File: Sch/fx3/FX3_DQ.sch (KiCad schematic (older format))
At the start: 22 parts, among them IC1 CYUSB3014, J1 JP4, J2 Header5, P1 CONN_02X40, P2 CONN_02X40, U1 LTC2292

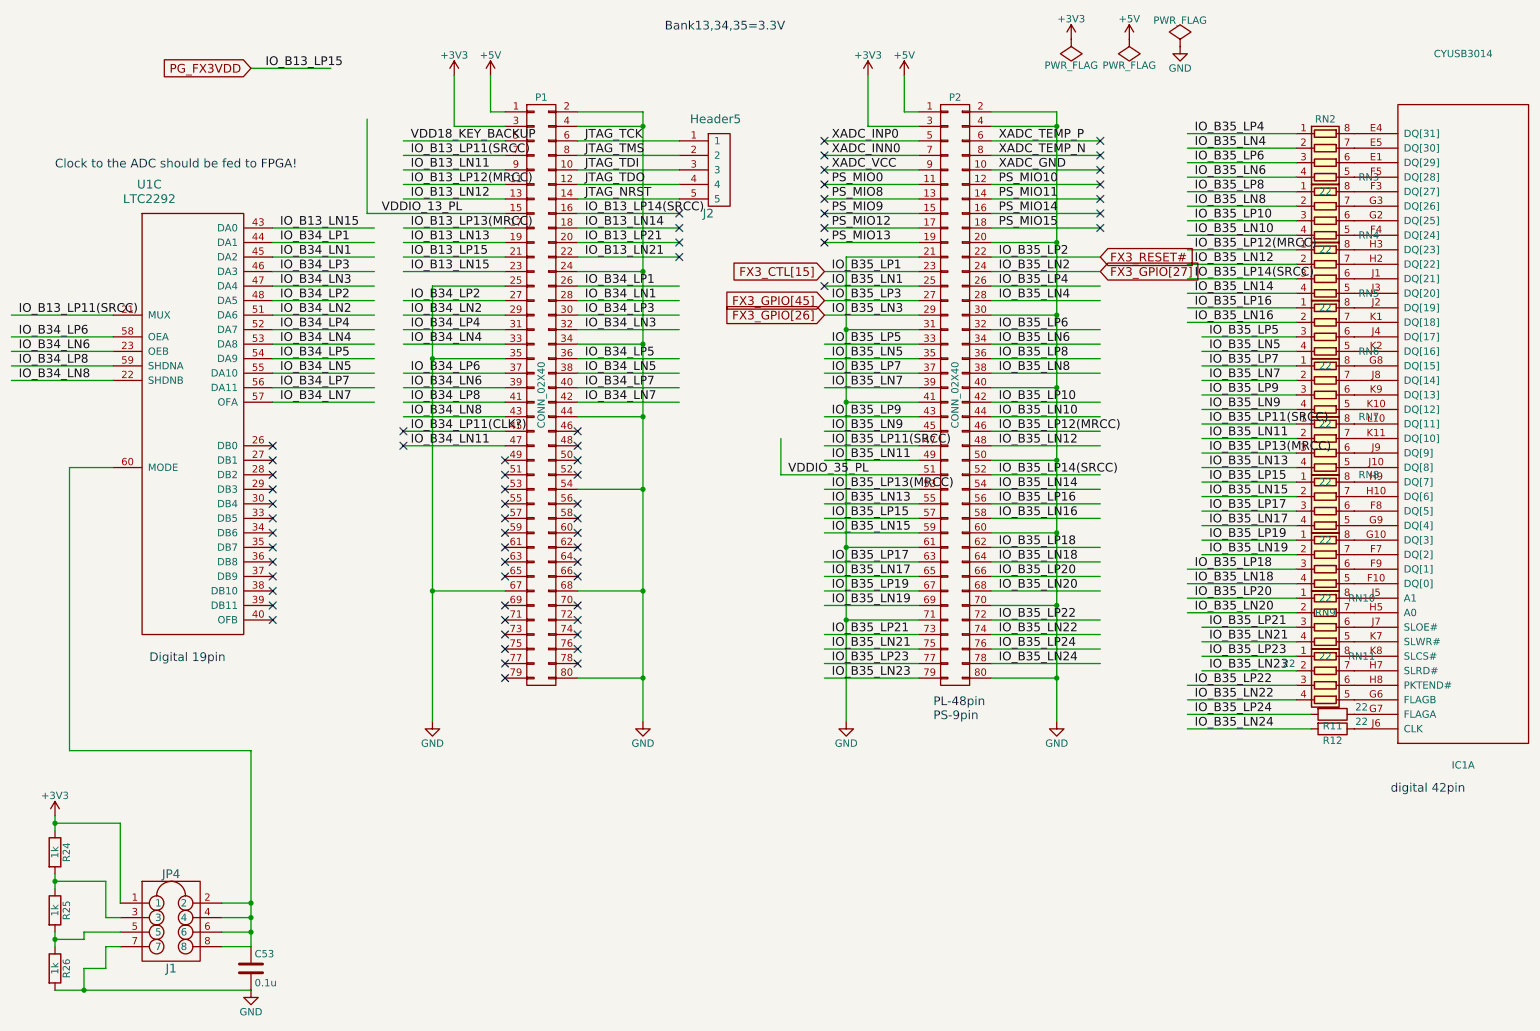
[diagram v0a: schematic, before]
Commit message: separate FX3 and ADC
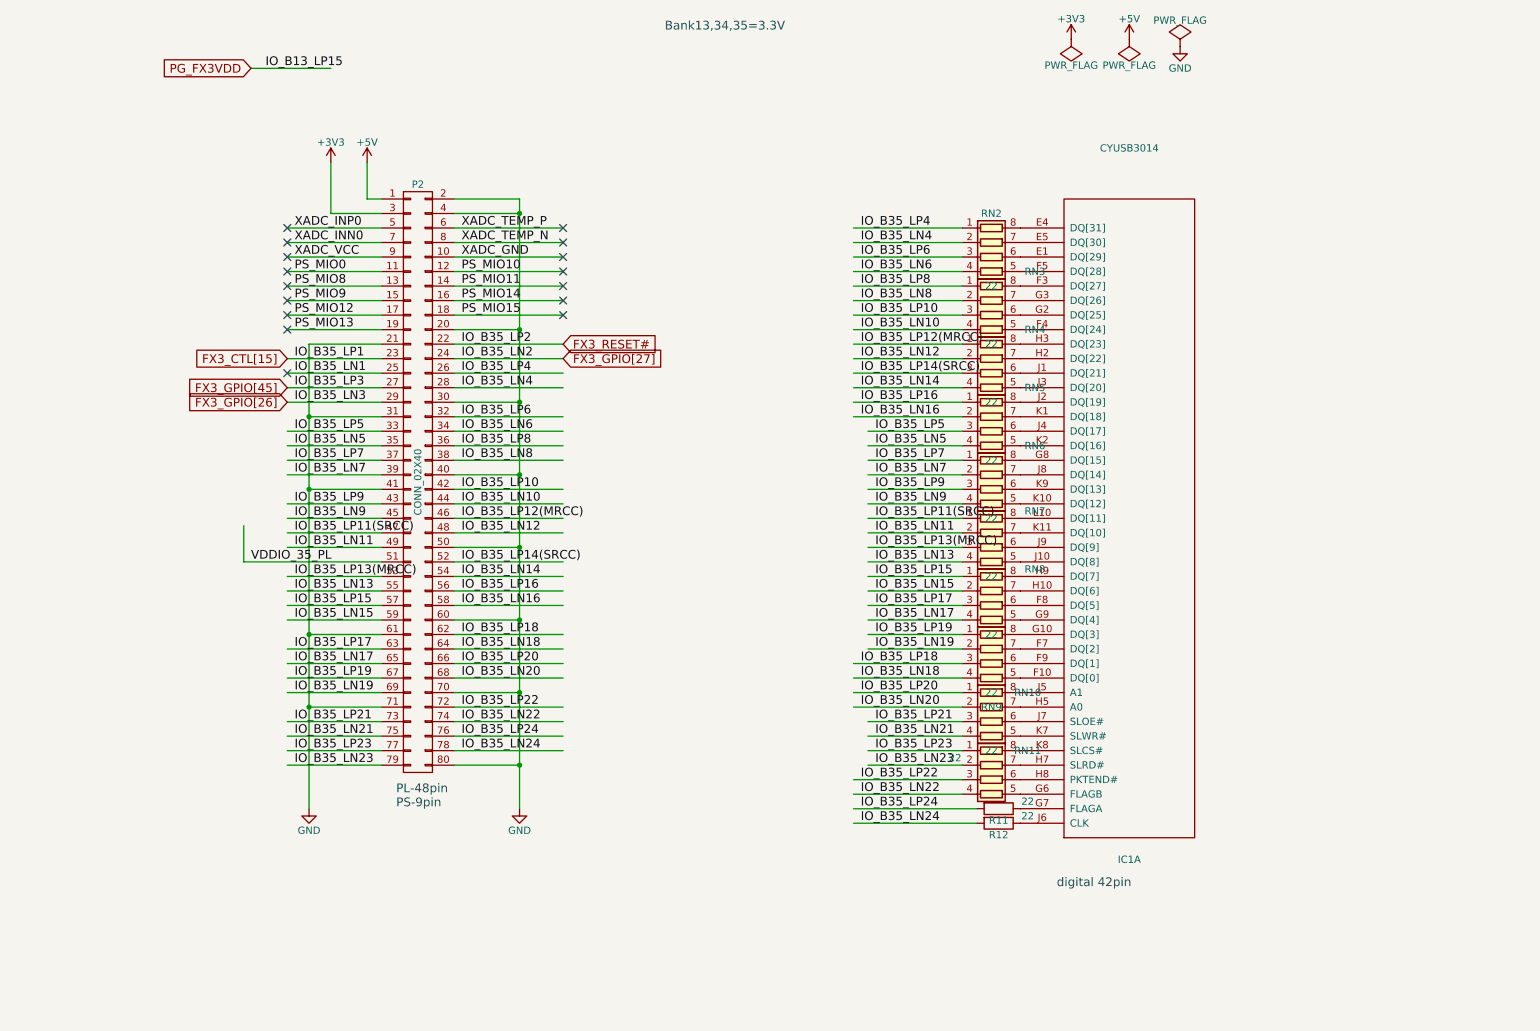
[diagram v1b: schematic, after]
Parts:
- removed C53: 0.1u, symbol C
- removed J1: JP4, symbol JP4
- removed J2: Header5, symbol Header5
- removed P1: CONN_02X40, symbol CONN_02X40
- removed R24, R25, R26: 1k, symbol R
- removed U1: LTC2292, symbol LTC2292
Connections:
- net labels removed: IO_B13_LN11, IO_B13_LN12, IO_B13_LN13, IO_B13_LN14, IO_B13_LN15, IO_B13_LN21, IO_B13_LP11(SRCC), IO_B13_LP12(MRCC), IO_B13_LP13(MRCC), IO_B13_LP14(SRCC), IO_B13_LP21, IO_B34_LN1, IO_B34_LN11, IO_B34_LN2, IO_B34_LN3, IO_B34_LN4, IO_B34_LN5, IO_B34_LN6, IO_B34_LN7, IO_B34_LN8, IO_B34_LP1, IO_B34_LP11(CLK?), IO_B34_LP2, IO_B34_LP3, IO_B34_LP4, IO_B34_LP5, IO_B34_LP6, IO_B34_LP7, IO_B34_LP8, JTAG_NRST, JTAG_TCK, JTAG_TDI, JTAG_TDO, JTAG_TMS, VDD18_KEY_BACKUP, VDDIO_13_PL
- wire segments 225 -> 128
- no-connect marks 65 -> 16
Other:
- note removed: "Clock to the ADC should be fed to FPGA!"
- note removed: "Digital 19pin"
- moved on the sheet: IC1A, P2, R11, R12, RN10, RN11, RN2, RN3, RN4, RN5, RN6, RN7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
